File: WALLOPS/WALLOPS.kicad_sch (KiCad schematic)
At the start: 20 parts, among them J1 JST-PH 1x8 Connector - WALLOP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, Q1 AO3401A, U1 VL53L8CX 0 (Zwicky), U2 VL58L8CX 1 (Aristotle), U3 VL53L8CX 3 (Copernicus), U4 VL53L8CX 2 (Brahe), U5 6DOF IMU (Sisko), U6 5V to 3.3V Converter

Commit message: Added updated WALLOPS PCB
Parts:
- removed TP2: 5V3.3_Test, RockSat:TestPoint_Pad_D2.0mm_With_Tolerance, symbol Connector:TestPoint
- C1: value 10µF -> 33µF
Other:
- moved on the sheet: U6
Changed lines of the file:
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@@
 	)
 	(junction
-		(at 148.59 43.18)
-		(diameter 0)
-		(color 0 0 0 0)
-	)
-	(junction
 		(at 90.17 81.28)
 		(diameter 0)
@@
 	(wire
 		(pts
-			(xy 185.42 40.64) (xy 247.65 40.64)
+			(xy 170.18 40.64) (xy 247.65 40.64)
 		)
 		(stroke
@@
 	(wire
 		(pts
-			(xy 137.16 43.18) (xy 148.59 43.18)
-		)
-		(stroke
-			(width 0)
-			(type default)
-		)
-	)
-	(wire
-		(pts
 			(xy 128.27 144.78) (xy 128.27 151.13)
 		)
@@
 	(wire
 		(pts
-			(xy 190.5 35.56) (xy 190.5 38.1)
+			(xy 175.26 35.56) (xy 175.26 38.1)
 		)
 		(stroke
@@
 	(wire
 		(pts
-			(xy 185.42 38.1) (xy 190.5 38.1)
+			(xy 170.18 38.1) (xy 175.26 38.1)
 		)
 		(stroke
@@
 	(wire
 		(pts
-			(xy 148.59 43.18) (xy 165.1 43.18)
+			(xy 137.16 43.18) (xy 149.86 43.18)
 		)
 		(stroke
@@
 	(wire
 		(pts
-			(xy 148.59 41.91) (xy 148.59 43.18)
-		)
-		(stroke
-			(width 0)
-			(type default)
-		)
-	)
-	(wire
-		(pts
 			(xy 64.77 68.58) (xy 64.77 81.28)
 		)
@@
 			)
 		)
-		(property "Value" "10µF"
+		(property "Value" "33µF"
 			(at 140.97 34.2899 0)
 			(effects
@@
 	(symbol
 		(lib_id "Connector:TestPoint")
-		(at 148.59 41.91 0)
-		(unit 1)
-		(exclude_from_sim no)
-		(in_bom yes)
-		(on_board yes)
-		(dnp no)
-		(property "Reference" "TP2"
-			(at 153.162 40.386 0)
-			(effects
-				(font
-					(size 1.27 1.27)
-				)
-				(justify right)
-			)
-		)
-		(property "Value" "5V3.3_Test"
-			(at 160.02 38.608 0)
-			(effects
-				(font
-					(size 1.27 1.27)
-				)
-				(justify right)
-			)
-		)
-		(property "Footprint" "RockSat:TestPoint_Pad_D2.0mm_With_Tolerance"
-			(at 153.67 41.91 0)
-			(effects
-				(font
-					(size 1.27 1.27)
-				)
-				(hide yes)
-			)
-		)
-		(property "Datasheet" "~"
-			(at 153.67 41.91 0)
-			(effects
-				(font
-					(size 1.27 1.27)
-				)
-				(hide yes)
-			)
-		)
-		(property "Description" "test point"
-			(at 148.59 41.91 0)
-			(effects
-				(font
-					(size 1.27 1.27)
-				)
-				(hide yes)
-			)
-		)
-		(pin "1"
-		)
-		(instances
-			(project ""
-				(path "/a71b320d-cbec-40c8-adfb-8ac61cfef5bf"
-					(reference "TP2")
-					(unit 1)
-				)
-			)
-		)
-	)
-	(symbol
-		(lib_id "Connector:TestPoint")
 		(at 60.96 101.6 180)
 		(unit 1)
@@
 	(symbol
 		(lib_id "RockSat_Sym:Pololu_D24V22F3")
-		(at 175.26 40.64 0)
+		(at 160.02 40.64 0)
 		(unit 1)
 		(exclude_from_sim no)
@@
 		(dnp no)
 		(property "Reference" "U6"
-			(at 175.26 28.956 0)
+			(at 160.02 28.956 0)
 			(effects
 				(font
@@
 		)
 		(property "Value" "5V to 3.3V Converter"
-			(at 175.768 31.496 0)
+			(at 160.528 31.496 0)
 			(effects
 				(font
@@
 		)
 		(property "Footprint" "RockSat:D24V22F3"
-			(at 175.26 40.64 0)
+			(at 160.02 40.64 0)
 			(effects
 				(font
@@
 		)
 		(property "Datasheet" ""
-			(at 175.26 40.64 0)
+			(at 160.02 40.64 0)
 			(effects
 				(font
@@
 		)
 		(property "Description" ""
-			(at 175.26 40.64 0)
+			(at 160.02 40.64 0)
 			(effects
 				(font
@@
 	(symbol
 		(lib_id "power:GND")
-		(at 190.5 35.56 180)
+		(at 175.26 35.56 180)
 		(unit 1)
 		(exclude_from_sim no)
@@
 		(fields_autoplaced yes)
 		(property "Reference" "#PWR02"
-			(at 190.5 29.21 0)
+			(at 175.26 29.21 0)
 			(effects
 				(font
@@
 		)
 		(property "Value" "GND"
-			(at 190.5 30.48 0)
+			(at 175.26 30.48 0)
 			(effects
 				(font
@@
 		)
 		(property "Footprint" ""
-			(at 190.5 35.56 0)
+			(at 175.26 35.56 0)
 			(effects
 				(font
@@
 		)
 		(property "Datasheet" ""
-			(at 190.5 35.56 0)
+			(at 175.26 35.56 0)
 			(effects
 				(font
@@
 		)
 		(property "Description" "Power symbol creates a global label with name \"GND\" , ground"
-			(at 190.5 35.56 0)
+			(at 175.26 35.56 0)
 			(effects
 				(font

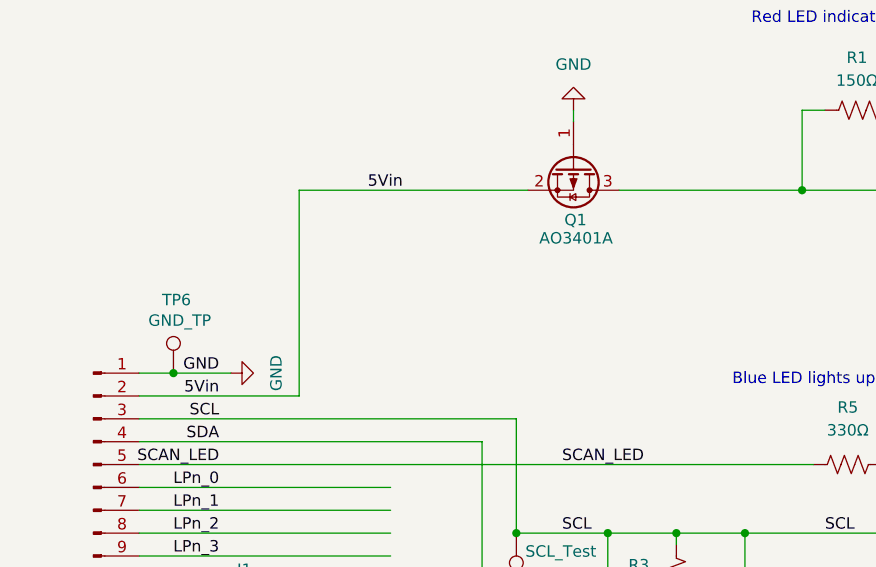
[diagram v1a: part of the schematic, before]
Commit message: Reduced size in WALLOPS
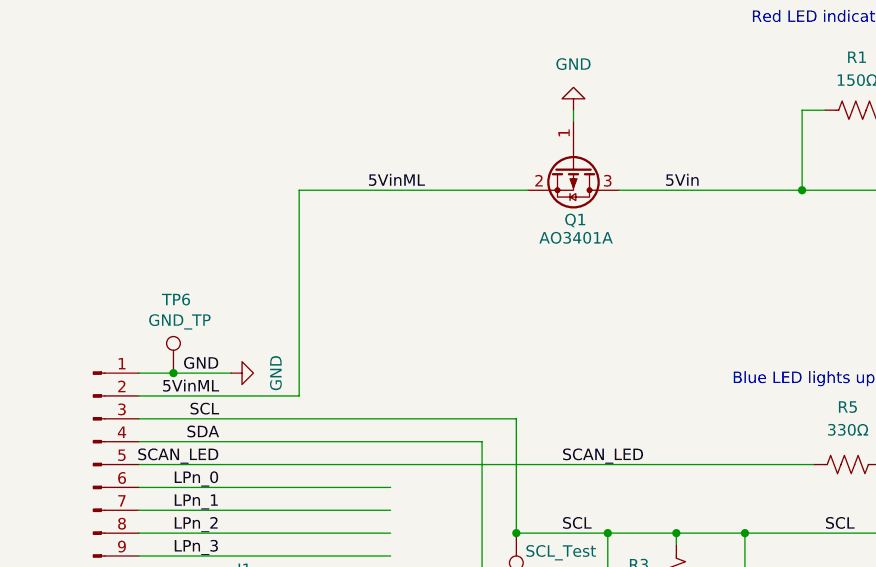
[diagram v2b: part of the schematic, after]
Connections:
- net 5Vin: no longer J1.2 (Pin_2), Q1.2 (S)
- new net 5VinML: J1.2 (Pin_2), Q1.2 (S)
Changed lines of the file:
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@@
 		)
 	)
-	(label "5Vin"
+	(label "5VinML"
 		(at 31.75 66.04 180)
 		(effects
@@
 		)
 	)
-	(label "5Vin"
+	(label "5VinML"
 		(at 48.26 43.18 0)
 		(effects
 			(font
+				(size 1.27 1.27)
+			)
+			(justify left bottom)
+		)
+	)
+	(label "5Vin"
+		(at 81.28 43.18 0)
+		(effects
+			(font

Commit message: Updated PCB
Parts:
- J1: value JST-PH 1x8 Connector - WALLOPS to ML Suite -> JST-PH 1x9 Connector - WALLOPS to ML Suite
- renumbered R3 to R2, R4 to R3, R5 to R4, TP6 to TP1, TP1 to TP2
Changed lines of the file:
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@@
 			)
 		)
-		(property "Value" "JST-PH 1x8 Connector - WALLOPS to ML Suite"
+		(property "Value" "JST-PH 1x9 Connector - WALLOPS to ML Suite"
 			(at 36.068 87.63 0)
 			(effects
@@
 		(dnp no)
 		(fields_autoplaced yes)
-		(property "Reference" "TP1"
-			(at 121.92 41.1481 0)
-			(effects
-				(font
-					(size 1.27 1.27)
-				)
-				(justify right)
+		(property "Reference" "TP2"
+			(at 127 38.6079 0)
+			(effects
+				(font
+					(size 1.27 1.27)
+				)
+				(justify left)
 			)
 		)
 		(property "Value" "5Vin_Test"
-			(at 121.92 38.6081 0)
-			(effects
-				(font
-					(size 1.27 1.27)
-				)
-				(justify right)
+			(at 127 41.1479 0)
+			(effects
+				(font
+					(size 1.27 1.27)
+				)
+				(justify left)
 			)
 		)
@@
 			(project ""
 				(path "/a71b320d-cbec-40c8-adfb-8ac61cfef5bf"
-					(reference "TP1")
+					(reference "TP2")
 					(unit 1)
 				)
@@
 		(on_board yes)
 		(dnp no)
-		(property "Reference" "R4"
+		(property "Reference" "R3"
 			(at 107.696 94.996 0)
 			(effects
@@
 			(project "WALLOPS"
 				(path "/a71b320d-cbec-40c8-adfb-8ac61cfef5bf"
-					(reference "R4")
+					(reference "R3")
 					(unit 1)
 				)
@@
 		(on_board yes)
 		(dnp no)
-		(property "Reference" "TP6"
+		(property "Reference" "TP1"
 			(at 25.4 55.372 0)
 			(effects
@@
 			(project "WALLOPS"
 				(path "/a71b320d-cbec-40c8-adfb-8ac61cfef5bf"
-					(reference "TP6")
+					(reference "TP1")
 					(unit 1)
 				)
@@
 		(on_board yes)
 		(dnp no)
-		(property "Reference" "R3"
+		(property "Reference" "R2"
 			(at 77.216 84.836 0)
 			(effects
@@
 			(project ""
 				(path "/a71b320d-cbec-40c8-adfb-8ac61cfef5bf"
-					(reference "R3")
+					(reference "R2")
 					(unit 1)
 				)
@@
 		(dnp no)
 		(fields_autoplaced yes)
-		(property "Reference" "R5"
+		(property "Reference" "R4"
 			(at 101.6 67.31 90)
 			(effects
@@
 			(project ""
 				(path "/a71b320d-cbec-40c8-adfb-8ac61cfef5bf"
-					(reference "R5")
-					(unit 1)
-				)
+					(reference "R4")
+					(unit 1)
+				)

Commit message: Reduced size of PCB
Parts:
- J1: footprint Connector_JST:JST_PH_B9B-PH-K_1x09_P2.00mm_Vertical -> Connector_JST:JST_PH_S9B-PH-K_1x09_P2.00mm_Horizontal
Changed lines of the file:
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@@
 			)
 		)
-		(property "Footprint" "Connector_JST:JST_PH_B9B-PH-K_1x09_P2.00mm_Vertical"
+		(property "Footprint" "Connector_JST:JST_PH_S9B-PH-K_1x09_P2.00mm_Horizontal"
 			(at 17.78 73.66 0)
 			(effects
